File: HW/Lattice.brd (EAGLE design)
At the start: 98 x 49 mm, 80 parts, among them IC2 LT1117-3,3V, IC5 LCMXO2-640, J1 CON_HEADER_2X05-PTH+SHROUDED_A, X1 MINI-USB-32005-201

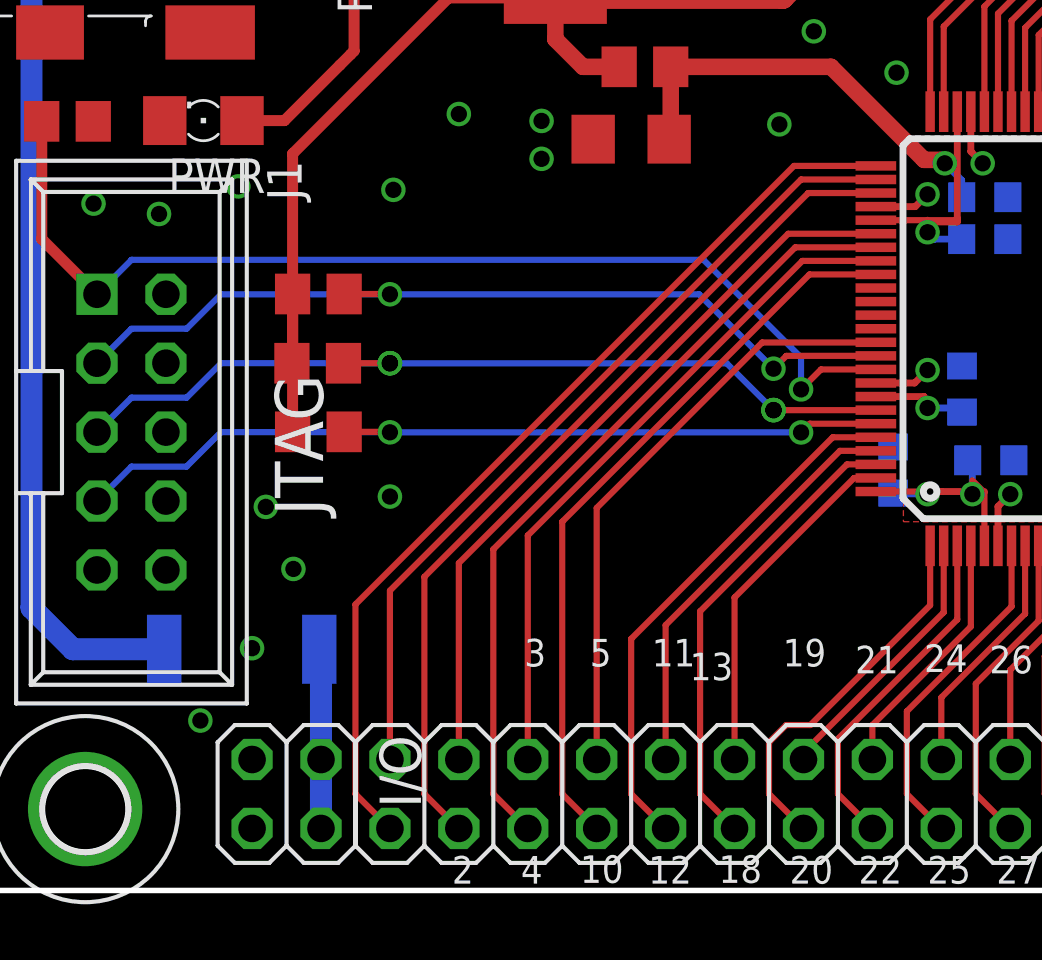
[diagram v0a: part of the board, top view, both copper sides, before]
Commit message: fix: connect programming pins prog and init, mirror schematic
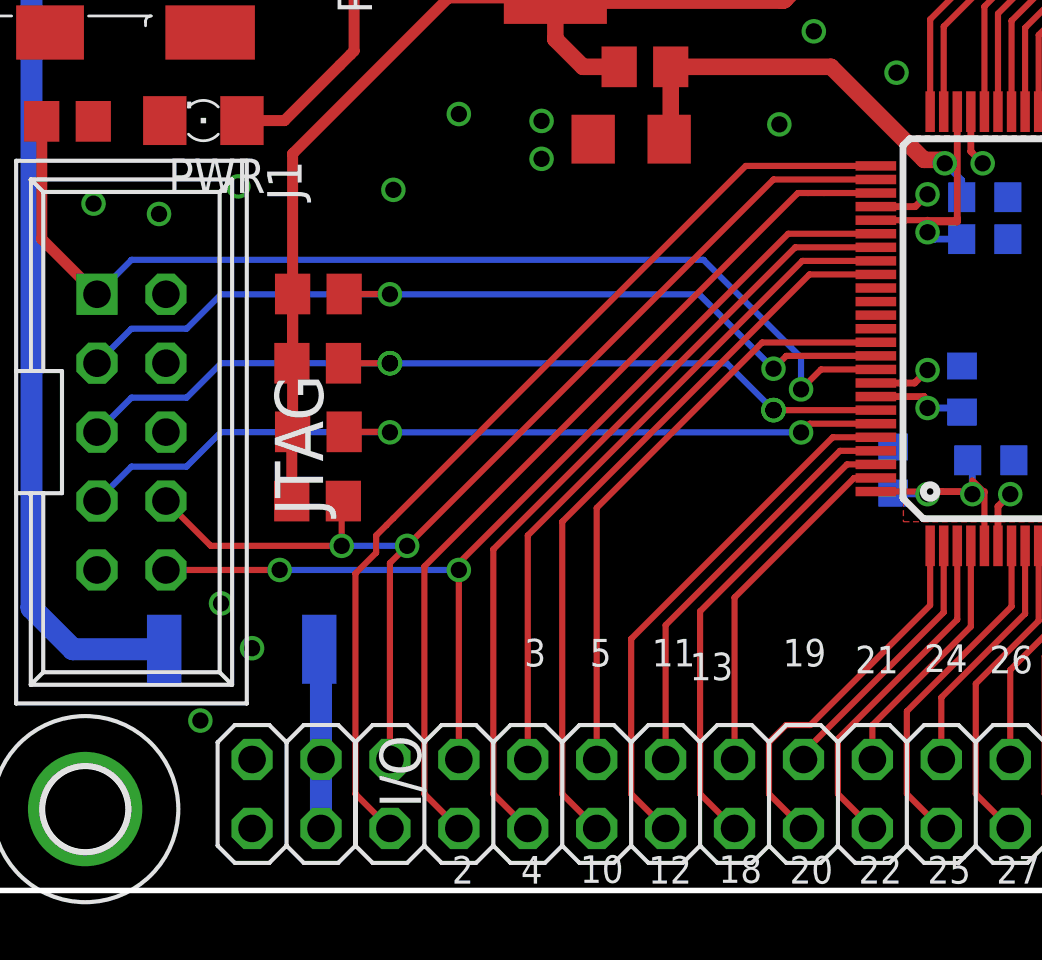
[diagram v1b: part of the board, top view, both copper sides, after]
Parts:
- added R30: 10k, rcl:R0805
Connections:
- removed net IO2: IC5.77, JP4.2
- removed net IO4: IC5.81, JP4.4
- new net IO2_INITN: IC5.77, J1.8, JP4.2, R30.1
- new net IO4_PROGRAMN: IC5.81, J1.10, JP4.4
- net +3V3: now also R30.2
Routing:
- net IO2_INITN: track 0.00 -> 42.3 mm, vias 0 -> 2
- net IO4_PROGRAMN: track 0.00 -> 38.4 mm, vias 0 -> 2
- net IO2: track 30.4 -> 0.00 mm
- net IO4: track 27.6 -> 0.00 mm
- net +3V3: track 214.1 -> 216.7 mm
- net IO1: track 34.7 -> 35.7 mm
- net GND: vias 60 -> 58
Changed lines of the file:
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@@
 <element name="D1" library="#PaJa_22" package="SM-1" value="1N4007_SM-1" x="9.271" y="8.89" smashed="yes" rot="MR180"/>
 <element name="D2" library="#PaJa_22" package="SM-1" value="1N4007_SM-1" x="9.271" y="40.894" smashed="yes" rot="MR180"/>
+<element name="R30" library="rcl" package="R0805" value="10k" x="12.065" y="14.351" smashed="yes" rot="R180"/>
 </elements>
 <signals>
@@
 <via x="6.223" y="24.9301" extent="1-16" drill="0.6"/>
 <via x="9.144" y="25.9461" extent="1-16" drill="0.6"/>
-<via x="10.16" y="14.1351" extent="1-16" drill="0.6"/>
-<via x="11.176" y="11.8491" extent="1-16" drill="0.6"/>
-<via x="14.732" y="14.5161" extent="1-16" drill="0.6"/>
+<via x="8.509" y="10.5791" extent="1-16" drill="0.6"/>
 <via x="14.859" y="25.8191" extent="1-16" drill="0.6"/>
 <via x="17.272" y="28.6131" extent="1-16" drill="0.6"/>
@@
 <wire x1="13.462" y1="3.556" x2="14.732" y2="2.286" width="0.2286" layer="1"/>
 <contactref element="IC5" pad="76"/>
-<wire x1="32.64" y1="26.701" x2="29.622" y2="26.701" width="0.2286" layer="1"/>
-<wire x1="13.462" y1="3.556" x2="13.462" y2="10.541" width="0.2286" layer="1"/>
-<wire x1="13.462" y1="10.541" x2="29.622" y2="26.701" width="0.2286" layer="1"/>
+<wire x1="32.64" y1="26.701" x2="27.844" y2="26.701" width="0.2286" layer="1"/>
+<wire x1="13.462" y1="3.556" x2="13.462" y2="11.684" width="0.2286" layer="1"/>
+<wire x1="13.462" y1="11.684" x2="14.224" y2="12.446" width="0.2286" layer="1"/>
+<wire x1="14.224" y1="12.446" x2="14.224" y2="13.081" width="0.2286" layer="1"/>
+<wire x1="14.224" y1="13.081" x2="14.605" y2="13.462" width="0.2286" layer="1"/>
+<wire x1="14.605" y1="13.462" x2="14.859" y2="13.716" width="0.2286" layer="1"/>
+<wire x1="27.844" y1="26.701" x2="14.859" y2="13.716" width="0.2286" layer="1"/>
 </signal>
 <signal name="IO3">
@@
 <wire x1="16.002" y1="3.556" x2="17.272" y2="2.286" width="0.2286" layer="1"/>
 <contactref element="IC5" pad="78"/>
-<wire x1="32.64" y1="25.701" x2="30.146" y2="25.701" width="0.2286" layer="1"/>
-<wire x1="16.002" y1="3.556" x2="16.002" y2="11.557" width="0.2286" layer="1"/>
-<wire x1="16.002" y1="11.557" x2="30.146" y2="25.701" width="0.2286" layer="1"/>
+<wire x1="32.64" y1="25.701" x2="30.734" y2="25.701" width="0.2286" layer="1"/>
+<wire x1="30.734" y1="25.701" x2="30.146" y2="25.701" width="0.2286" layer="1"/>
+<wire x1="16.002" y1="3.556" x2="16.002" y2="11.938" width="0.2286" layer="1"/>
+<wire x1="16.002" y1="11.938" x2="29.765" y2="25.701" width="0.2286" layer="1"/>
+<wire x1="29.765" y1="25.701" x2="30.146" y2="25.701" width="0.2286" layer="1"/>
 </signal>
 <signal name="IO5">
@@
 <wire x1="24.892" y1="4.826" x2="24.892" y2="9.779" width="0.2286" layer="1"/>
 <wire x1="24.892" y1="9.779" x2="31.314" y2="16.201" width="0.2286" layer="1"/>
-</signal>
-<signal name="IO4">
-<contactref element="JP4" pad="4"/>
-<contactref element="IC5" pad="81"/>
-<wire x1="32.64" y1="24.201" x2="29.408" y2="24.201" width="0.2286" layer="1"/>
-<wire x1="17.272" y1="4.826" x2="17.272" y2="12.065" width="0.2286" layer="1"/>
-<wire x1="17.272" y1="12.065" x2="29.408" y2="24.201" width="0.2286" layer="1"/>
-</signal>
-<signal name="IO2">
-<contactref element="JP4" pad="2"/>
-<contactref element="IC5" pad="77"/>
-<wire x1="32.64" y1="26.201" x2="29.884" y2="26.201" width="0.2286" layer="1"/>
-<wire x1="14.732" y1="4.826" x2="14.732" y2="11.049" width="0.2286" layer="1"/>
-<wire x1="14.732" y1="11.049" x2="29.884" y2="26.201" width="0.2286" layer="1"/>
 </signal>
 <signal name="N$27">
@@
 <wire x1="88.5642" y1="40.815" x2="85.9033" y2="40.815" width="0.6096" layer="1"/>
 <wire x1="85.9033" y1="40.815" x2="85.6096" y2="41.1087" width="0.6096" layer="1"/>
+<contactref element="R30" pad="2"/>
+<wire x1="11.1458" y1="16.9018" x2="11.115" y2="16.9018" width="0.4064" layer="1"/>
+<wire x1="11.115" y1="16.9018" x2="11.115" y2="14.351" width="0.4064" layer="1"/>
 <wire x1="85.598" y1="45.1108" x2="85.6096" y2="44.5912" width="0" layer="19" extent="1-1"/>
 <wire x1="20.828" y1="32.934" x2="20.828" y2="32.893" width="0" layer="19" extent="1-1"/>
@@
 <wire x1="9.017" y1="37.973" x2="7.366" y2="37.973" width="0.508" layer="1"/>
 </signal>
+<signal name="IO2_INITN">
+<contactref element="IC5" pad="77"/>
+<contactref element="JP4" pad="2"/>
+<contactref element="J1" pad="8"/>
+<wire x1="28.868" y1="26.201" x2="32.64" y2="26.201" width="0.2286" layer="1"/>
+<contactref element="R30" pad="1"/>
+<wire x1="6.477" y1="14.351" x2="8.128" y2="12.7" width="0.2286" layer="1"/>
+<wire x1="14.732" y1="12.065" x2="14.732" y2="4.826" width="0.2286" layer="1"/>
+<via x="15.367" y="12.7" extent="1-16" drill="0.6"/>
+<wire x1="8.128" y1="12.7" x2="12.954" y2="12.7" width="0.2286" layer="1"/>
+<via x="12.954" y="12.7" extent="1-16" drill="0.6"/>
+<wire x1="12.954" y1="12.7" x2="15.367" y2="12.7" width="0.2286" layer="16"/>
+<wire x1="13.015" y1="14.351" x2="12.954" y2="14.351" width="0.2286" layer="1"/>
+<wire x1="12.954" y1="14.351" x2="12.954" y2="12.7" width="0.2286" layer="1"/>
+<wire x1="14.732" y1="12.065" x2="15.367" y2="12.7" width="0.2286" layer="1"/>
+<wire x1="28.868" y1="26.201" x2="15.367" y2="12.7" width="0.2286" layer="1"/>
+</signal>
+<signal name="IO4_PROGRAMN">
+<contactref element="IC5" pad="81"/>
+<contactref element="JP4" pad="4"/>
+<wire x1="17.272" y1="4.826" x2="17.272" y2="11.811" width="0.2286" layer="1"/>
+<wire x1="17.272" y1="11.811" x2="17.272" y2="12.065" width="0.2286" layer="1"/>
+<wire x1="17.272" y1="12.065" x2="29.408" y2="24.201" width="0.2286" layer="1"/>
+<contactref element="J1" pad="10"/>
+<wire x1="29.408" y1="24.201" x2="32.64" y2="24.201" width="0.2286" layer="1"/>
+<via x="10.668" y="11.811" extent="1-16" drill="0.6"/>
+<via x="17.272" y="11.811" extent="1-16" drill="0.6"/>
+<wire x1="10.668" y1="11.811" x2="17.272" y2="11.811" width="0.2286" layer="16"/>
+<wire x1="6.477" y1="11.811" x2="10.668" y2="11.811" width="0.2286" layer="1"/>
+</signal>
 </signals>
